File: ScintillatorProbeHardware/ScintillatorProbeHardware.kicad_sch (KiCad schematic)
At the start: 95 parts, among them J1 USB_B, J2 Conn_01x02, J3 Conn_01x03, J4 Conn_01x04, Q1 15N10, Q2 S8050, Q3 2N2222A, Q4 AO401, Q5 2N2222A, Q6 2N2222A, T1 24:1800, U1 ICL7660, U2 LM4562, U3 LM358, U4 STM32F103C8Tx, U5 USBLC6-2SC6, U6 AMS1117-3.3, U7 LM318N, U8 LM318N, U9 LM318N, Y1 32.768kHz, Y2 8MHz

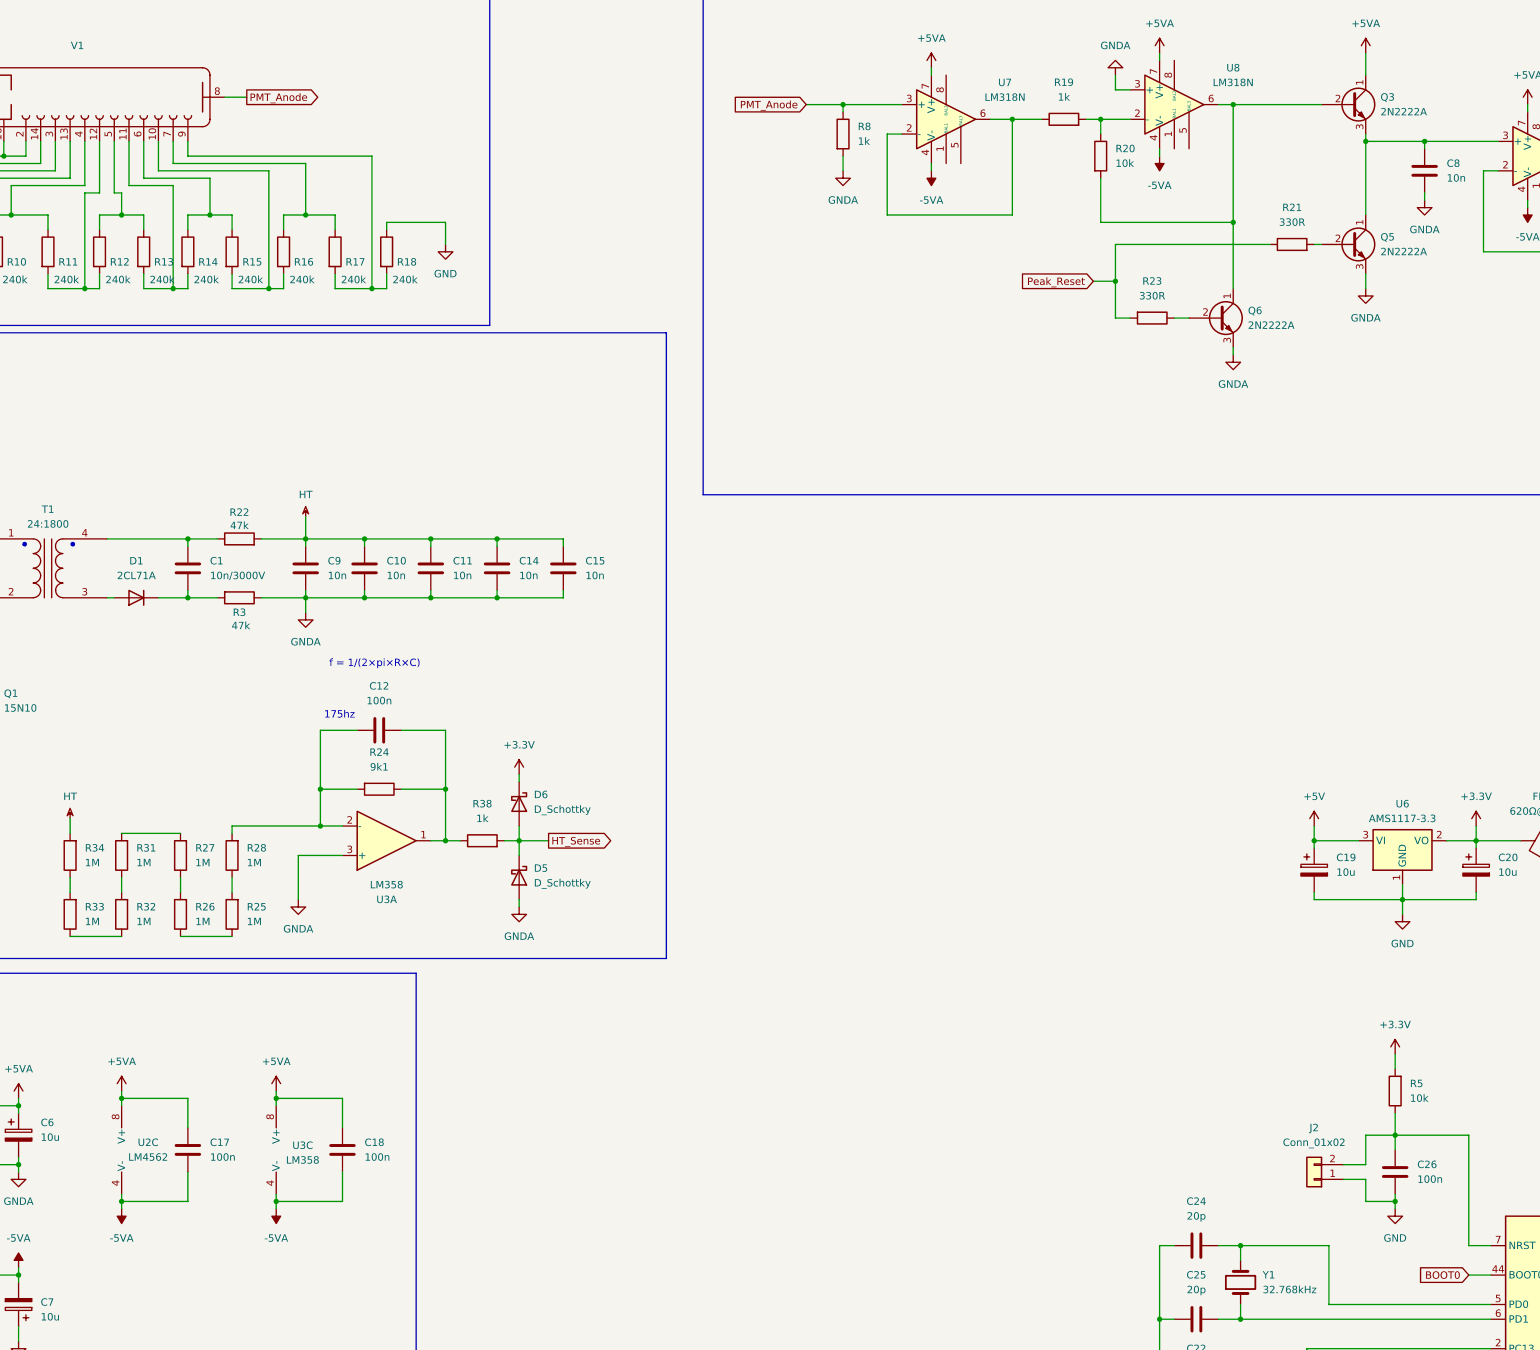
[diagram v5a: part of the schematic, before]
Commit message: PCB layout started, firmware modified for new peak detector
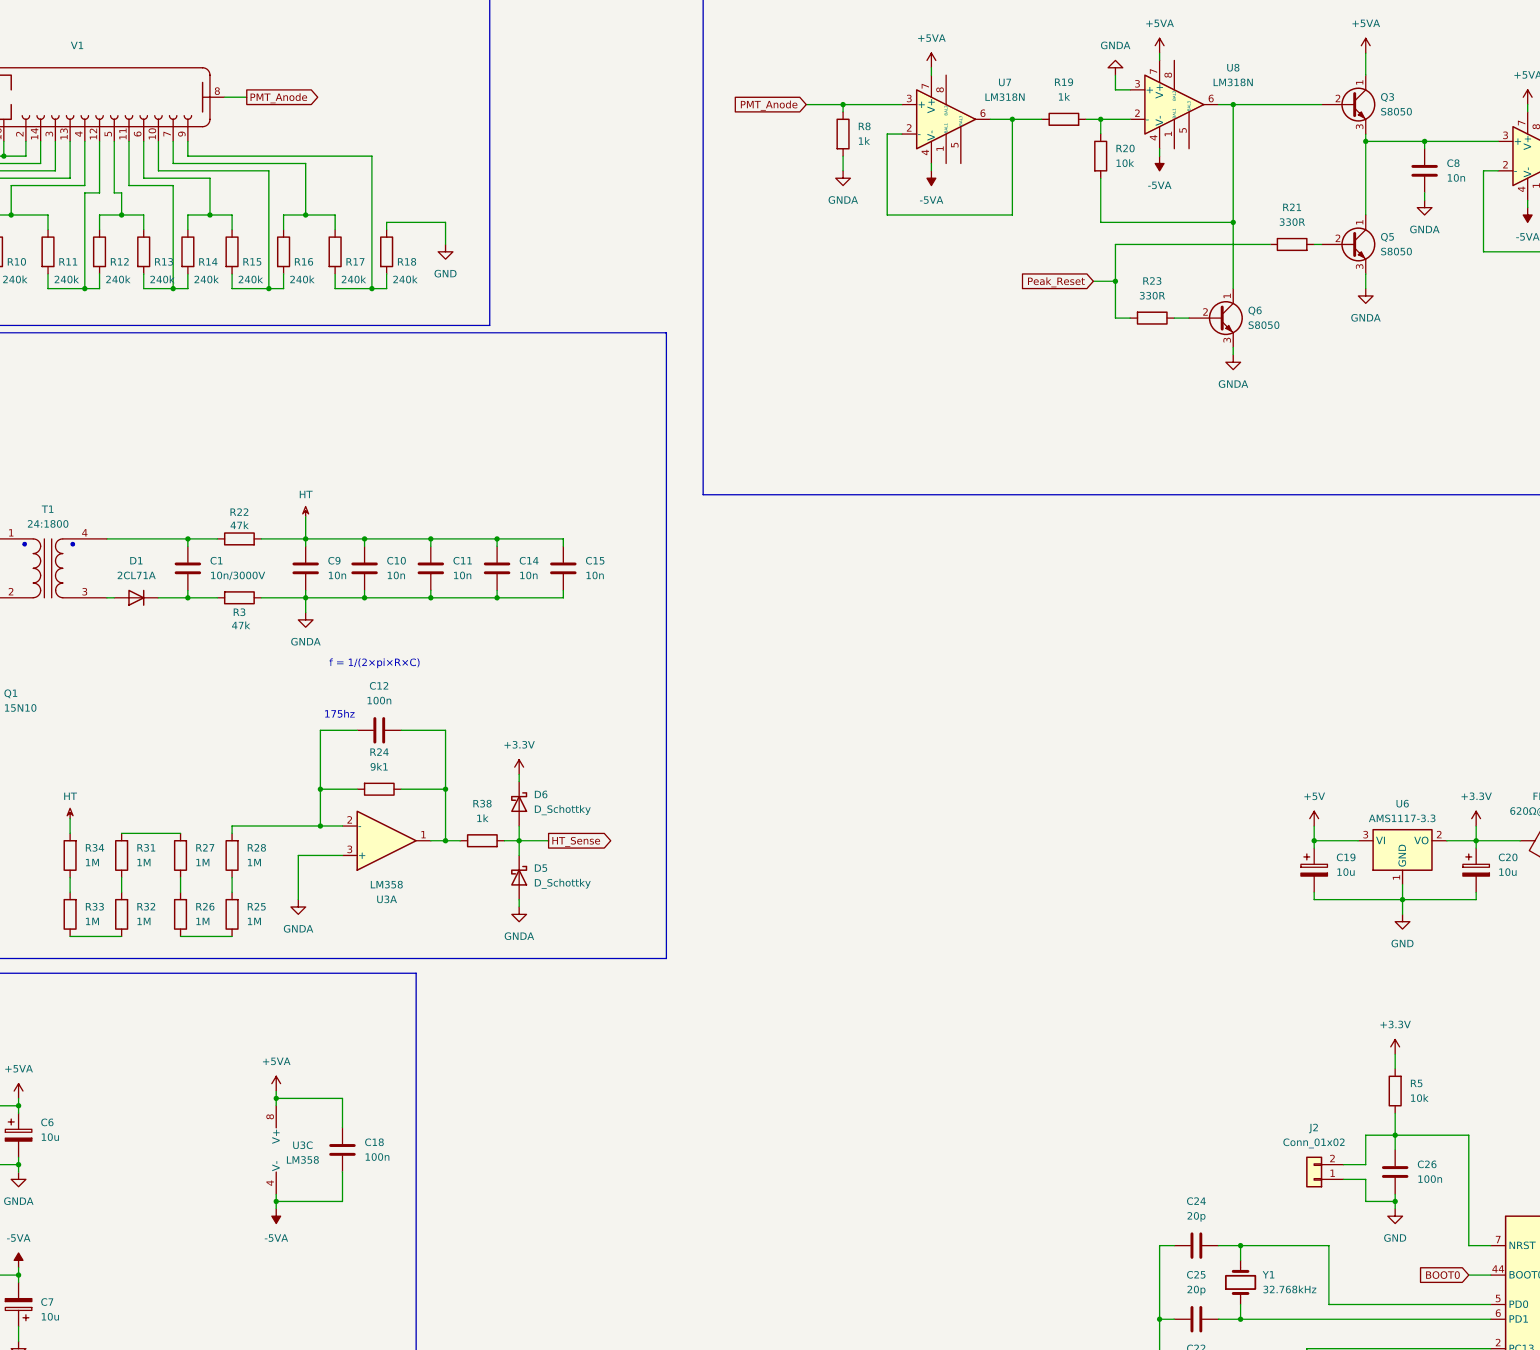
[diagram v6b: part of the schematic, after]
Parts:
- removed C17: 100n, Capacitor_SMD:C_0603_1608Metric, symbol Device:C
- removed U2: LM4562, symbol Amplifier_Operational:LM4562
- C1, C10, C11, C14, C15, C9: footprint (none) -> Capacitor_THT:C_Disc_D16.0mm_W5.0mm_P7.50mm
- C8: footprint (none) -> Capacitor_SMD:C_0603_1608Metric; LCSC (none) -> https://www.lcsc.com/product-detail/Multilayer-Ceramic-Capa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; LCSC Part Number (none) -> C14663
- D1: footprint (none) -> Diode_THT:D_A-405_P12.70mm_Horizontal
- D2, D3: footprint (none) -> Diode_SMD:D_SOD-523; LCSC (none) -> https://www.lcsc.com/product-detail/Schottky-Diodes_onsemi-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; LCSC Part Number (none) -> C145179
- J4: footprint (none) -> Connector_PinHeader_2.54mm:PinHeader_1x04_P2.54mm_Vertical
- Q3, Q5, Q6: value 2N2222A -> S8050; footprint (none) -> Package_TO_SOT_SMD:SOT-23; LCSC (none) -> https://www.lcsc.com/product-detail/Bipolar-BJT_Guangdong-H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; LCSC Part Number (none) -> C181158
- R19, R35, R8: footprint (none) -> Resistor_SMD:R_0603_1608Metric; LCSC (none) -> https://www.lcsc.com/product-detail/Chip-Resistor-Surface-M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; LCSC Part Number (none) -> C21190
- R20: footprint (none) -> Resistor_SMD:R_0603_1608Metric; LCSC (none) -> https://www.lcsc.com/product-detail/Chip-Resistor-Surface-M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; LCSC Part Number (none) -> C25804
- R21, R23: footprint (none) -> Resistor_SMD:R_1812_4532Metric; LCSC (none) -> https://www.lcsc.com/product-detail/Chip-Resistor-Surface-M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; LCSC Part Number (none) -> C2933950
- U7, U8, U9: LCSC (none) -> https://www.lcsc.com/product-detail/Operational-Amplifier_T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; LCSC Part Number (none) -> C1347395

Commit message: PCB mostly routed
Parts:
- added C17, C27, C28, C29, C30, C31, C32: 1u, Capacitor_SMD:C_0603_1608Metric, symbol Device:C
- added H1, H2, H3, H4: MountingHole, MountingHole:MountingHole_3.2mm_M3_Pad, symbol Mechanical:MountingHole
- added J5, J6: ~, Connector_PinHeader_2.54mm:PinHeader_1x02_P2.54mm_Vertical, symbol Connector_Generic:Conn_01x02
- added J7: Conn_01x02, Connector_PinHeader_2.54mm:PinHeader_1x02_P2.54mm_Vertical, symbol Connector_Generic:Conn_01x02
- added Q7: S8050, Package_TO_SOT_SMD:SOT-23, symbol Device:Q_NPN_CBE
- added R36, R39: 1k, Resistor_SMD:R_0603_1608Metric, symbol Device:R
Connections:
- net +3.3V: now also U5.5 (VBUS), C29.2, C31.2, C32.2; no longer D6.1 (K)
- net +3.3VA: now also D6.1 (K), C30.2
- net +5V: now also J7.1 (Pin_1), R39.1; no longer U5.5 (VBUS)
- net +5VA: now also C17.2, C27.2, C28.2
- net -5VA: now also C17.1, C27.1, C28.1
- net GND: now also C29.1, C31.1, C32.1, Q7.3 (E); no longer R18.1
- net GNDA: now also C30.1
- net HT: now also J6.1 (Pin_1); no longer R1.2, V1.20 (Photocatode)
- net HT_Drive_Pulse: now also U4.29 (PA8)
- net HT_Sense: now also U4.10 (PA0)
- net PMT_Anode: now also J6.2 (Pin_2); no longer V1.8 (Anode)
- net Peak_Reset: now also U4.16 (PA6)
- net Peak_Sense: now also U4.11 (PA1)
- net Buzzer: now reaches U4.13 (PA3)
- net Buzzer: now also R36.2
- new net: J5.1 (Pin_1), R1.2, V1.20 (Photocatode)
- new net: Q7.2 (B), R36.1
- new net: J7.2 (Pin_2), Q7.1 (C), R39.2
- new net: J5.2 (Pin_2), R18.1, V1.8 (Anode)

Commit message: Added USB connector, some loops on PCB optimized
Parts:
- added J8: Conn_01x03, Connector_PinHeader_2.54mm:PinHeader_1x03_P2.54mm_Vertical, symbol Connector_Generic:Conn_01x03
- added J9: Conn_01x01, Connector_PinHeader_2.54mm:PinHeader_1x01_P2.54mm_Vertical, symbol Connector_Generic:Conn_01x01
- J1: footprint (none) -> CustomParts:Amphenol_USB_B; TME (none) -> https://www.tme.eu/cz/details/tueb4f2d0b/konektory-usb-a-ie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
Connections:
- net +5V: now also J8.1 (Pin_1)
- net GND: now also J1.5 (Shield), J8.3 (Pin_3)
- net GNDA: now also J6.1 (Pin_1)
- net HT: now also J9.1 (Pin_1); no longer J6.1 (Pin_1)
- net HT_Power: now also J8.2 (Pin_2)
- net usb_P: now reaches J1.3 (D+), U5.1 (I/O1)
- net usb_N: now reaches J1.2 (D-), U5.3 (I/O2)
